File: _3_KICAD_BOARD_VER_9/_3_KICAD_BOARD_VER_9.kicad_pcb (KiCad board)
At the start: 2 copper layers, 62.2 x 50 mm, 36 parts, among them J1 PH2-20-UA, U1 AZ1117H-3.3TRE1, U2 dsPIC33AK512MPS505T-I/PT, U3 DAC7564ICPW, U4 FM24W256G, Y1 ABMM-25.000MHZ-B2-T

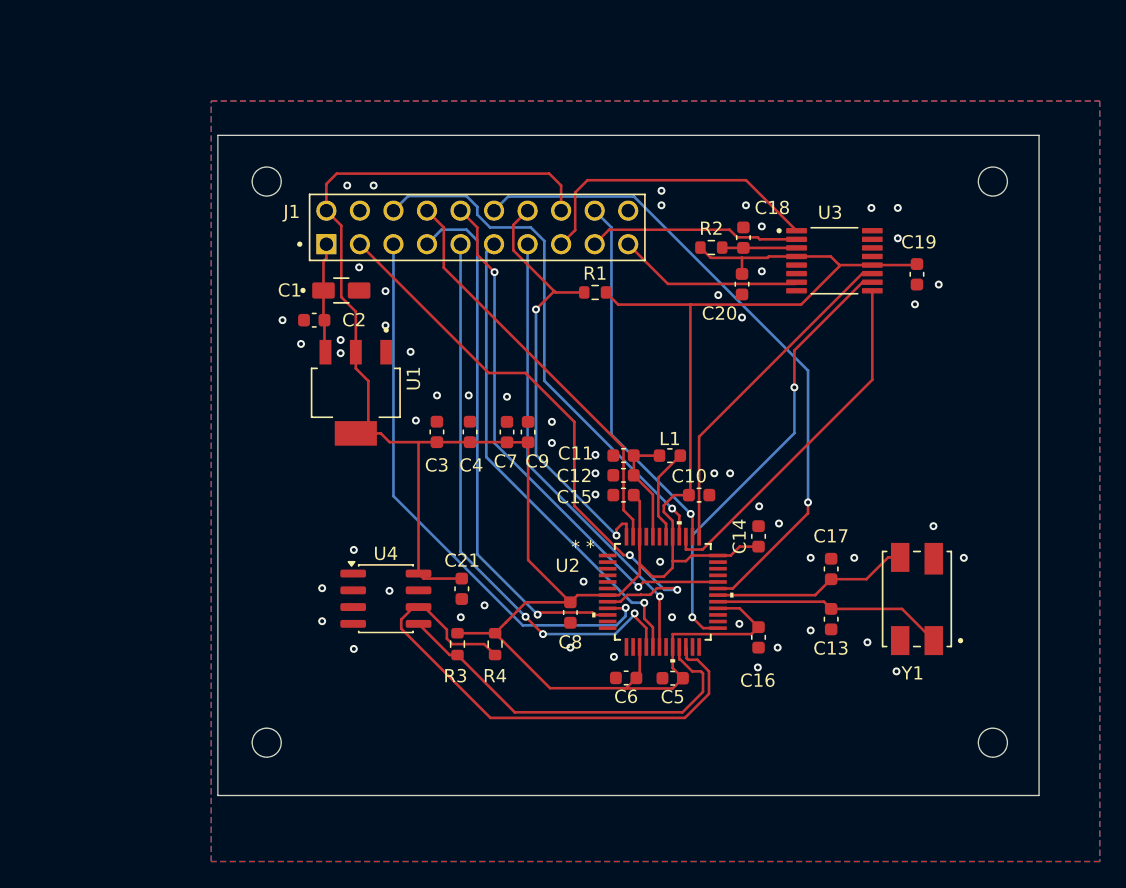
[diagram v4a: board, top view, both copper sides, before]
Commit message: feat : 회로도 업데이트
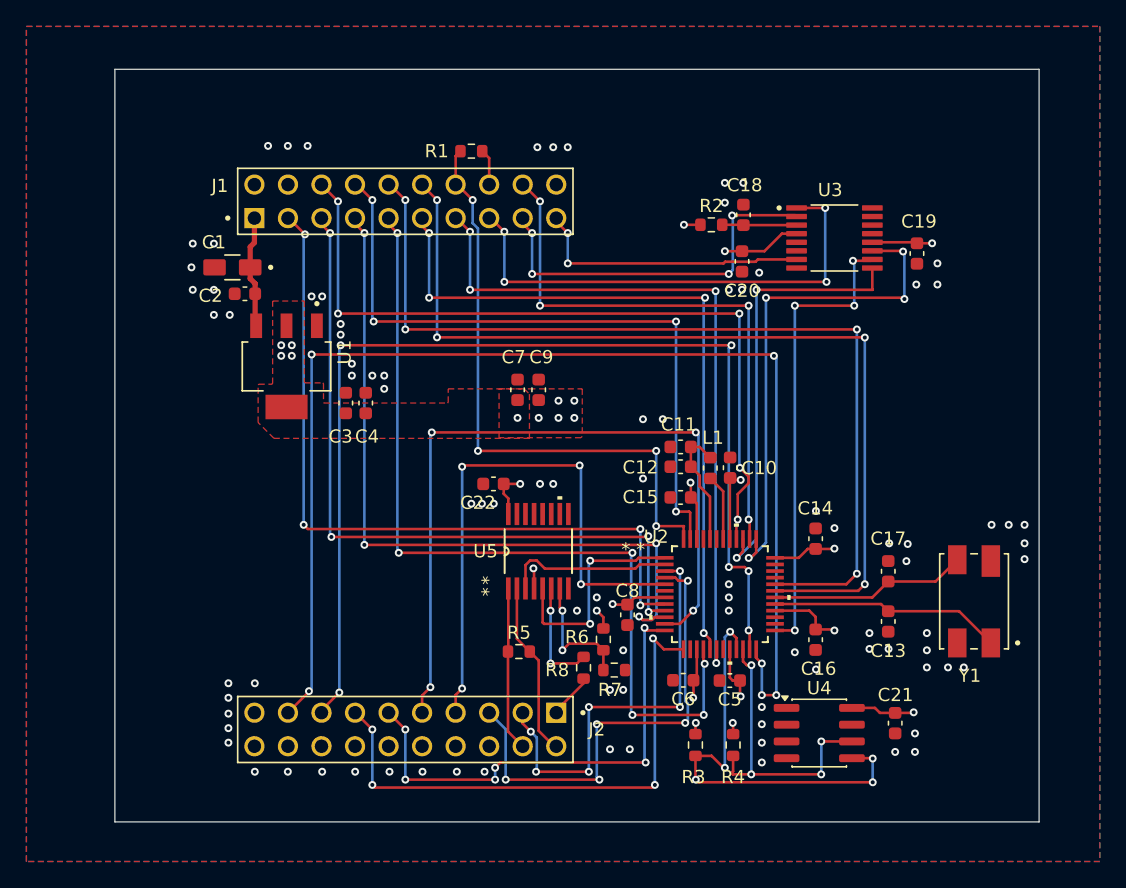
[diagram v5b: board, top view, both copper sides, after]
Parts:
- removed REF** (x4): MountingHole_2.2mm_M2, MountingHole:MountingHole_2.2mm_M2
- added C22: 100nF, Capacitor_SMD:C_0603_1608Metric, F.Cu at (103.7, 76.4)
- added J2: PH2-20-UA, PH2-20-UA:ADAM_PH2-20-UA, F.Cu at (97.0, 95.0)
- added R5: 100R, Resistor_SMD:R_0603_1608Metric, F.Cu at (105.6, 89.1)
- added R6: 12K, Resistor_SMD:R_0603_1608Metric, F.Cu at (112.0, 88.2)
- added R7: 10K, Resistor_SMD:R_0603_1608Metric, F.Cu at (112.8, 90.5)
- added R8: 100R, Resistor_SMD:R_0603_1608Metric, F.Cu at (110.5, 90.3)
- added U5: AM26LV32EIPWR, AMP26LV32EIPWR:PW16, F.Cu at (107.1, 81.5)
- moved C21 34.4 mm to (134.1, 94.5)
- moved U4 34.4 mm to (128.3, 95.3)
- moved R4 19.6 mm to (121.8, 96.2)
- moved R3 19.6 mm to (119.0, 96.2)
- moved R1 14.2 mm to (102.0, 51.2)
- moved C1 8.43 mm to (83.9, 60.0), turned to 180 degrees
- moved C4 8.20 mm to (94.0, 70.3)
- moved C3 7.24 mm to (92.5, 70.3)
- moved J1 5.80 mm to (97.0, 55.0)
- moved C2 5.62 mm to (84.8, 62.0)
- moved U1 5.62 mm to (88.0, 67.5)
- moved C11 4.37 mm to (117.8, 73.6)
- moved C12 4.37 mm to (117.8, 75.1)
- moved C13 4.33 mm to (133.6, 86.8)
- moved C14 4.33 mm to (128.1, 80.6)
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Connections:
- U2 pad 1: unconnected-(U2-PGD2/AD3AN5/CVDAN0/CMP6A/RP1/SCL2/IOMAF2/RA0-Pad1) -> /MCU_48PIN_SHEET/PULSE_GATE_BUS.SINGLE_SIGNAL_3_3V
- U2 pad 11: unconnected-(U2-OA3OUT/AD3AN0/CVDAN5/CMP3A/RP6/INT0/RA5-Pad11) -> /MCU_48PIN_SHEET/AUX_BUS.3
- U2 pad 12: unconnected-(U2-OA3IN-/AD3ANN2/AD3AN2/CVDAN6/CMPDN/CMP3C/RP7/RA6-Pad12) -> /MCU_48PIN_SHEET/AUX_BUS.4
- U2 pad 13: unconnected-(U2-OA3IN+/AD3AN1/AD4AN5/CVDAN21/CVDTX5/CMP3B/RP22/RB5-Pad13) -> /MCU_48PIN_SHEET/AUX_BUS.5
- U2 pad 2: unconnected-(U2-AD5ANN1/AD5AN0/CVDAN7/CMP6B/RP8/SDA2/IOMAF1/RA7-Pad2) -> /MCU_48PIN_SHEET/PULSE_GATE_BUS.DIFF_SIGNAL_3_3V
- U2 pad 23: unconnected-(U2-AD4ANN2/AD4AN1/CVDAN22/CVDTX6/CMP/CMP7D/IBIAS0/ISRC0/RP23/RB6-Pad23) -> /MCU_48PIN_SHEET/AUX_BUS.6
- U2 pad 24: unconnected-(U2-AD4ANN1/AD4AN2/CVDAN23/CVDTX7/CMP4C/IBIAS1/ISRC1/RP24/IOMAF0/RB7-Pad24) -> /MCU_48PIN_SHEET/AUX_BUS.7
- U2 pad 3: unconnected-(U2-PGC2/DACOUT1/AD5AN1/CVDAN1/CMP4D/RP2/RA1-Pad3) -> /MCU_48PIN_SHEET/AUX_BUS.0
- U2 pad 4: unconnected-(U2-DACOUT2/AD5AN3/CVDAN8/CMP5A/IBIAS3/ISRC3/RP9/RA8-Pad4) -> /MCU_48PIN_SHEET/AUX_BUS.1
- U2 pad 5: unconnected-(U2-UREF/AD1AN3/CVDAN9/CMP5B/CMP7A/IBIAS2/ISRC2/RP10/RA9-Pad5) -> /MCU_48PIN_SHEET/AUX_BUS.2
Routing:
- net +3.3V: track 207.7 -> 60.8 mm, vias 0 -> 26
- net /MCU_48PIN_SHEET/AUX_BUS.7: track 0.00 -> 93.5 mm, vias 0 -> 6
- net /MCU_48PIN_SHEET/AUX_BUS.6: track 0.00 -> 82.5 mm, vias 0 -> 6
- net /MCU_48PIN_SHEET/AUX_BUS.3: track 0.00 -> 57.8 mm, vias 0 -> 4
- net /MCU_48PIN_SHEET/AUX_BUS.2: track 0.00 -> 43.2 mm, vias 0 -> 4
- net /MCU_48PIN_SHEET/AUX_BUS.5: track 0.00 -> 41.4 mm, vias 0 -> 4
- net /MCU_48PIN_SHEET/AUX_BUS.4: track 0.00 -> 36.7 mm, vias 0 -> 6
- net /MCU_48PIN_SHEET/AUX_BUS.1: track 0.00 -> 36.6 mm, vias 0 -> 5
- net /MCU_48PIN_SHEET/AUX_BUS.0: track 0.00 -> 32.2 mm, vias 0 -> 6
- net /MCU_48PIN_SHEET/DEBUG_BUS.PGD: track 40.3 -> 70.8 mm, vias 2 -> 4
- net /MCU_48PIN_SHEET/ADC_BUS._B0: track 42.7 -> 66.2 mm, vias 3 -> 6
- net /MCU_48PIN_SHEET/DEBUG_BUS.PGC: track 49.7 -> 70.1 mm, vias 1 -> 4
- net /MCU_48PIN_SHEET/UART_BUS.RX: track 31.2 -> 51.4 mm, vias 0 -> 4
- net /MCU_48PIN_SHEET/ADC_BUS._B2: track 34.7 -> 53.8 mm, vias 1 -> 4
- net /MCU_48PIN_SHEET/I2C_BUS.SCL: track 41.6 -> 22.9 mm, vias 0 -> 4
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- added copper zone on F.Cu, net +3.3V
- added copper zone on In2.Cu, net +3.3V
- added copper zone on In1.Cu, net GND
- added copper zone on In2.Cu, net GND
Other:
- board size 62.2 x 50 mm -> 70 x 57 mm
- copper layers 2 -> 4
